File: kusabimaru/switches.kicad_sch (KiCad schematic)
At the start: 276 parts

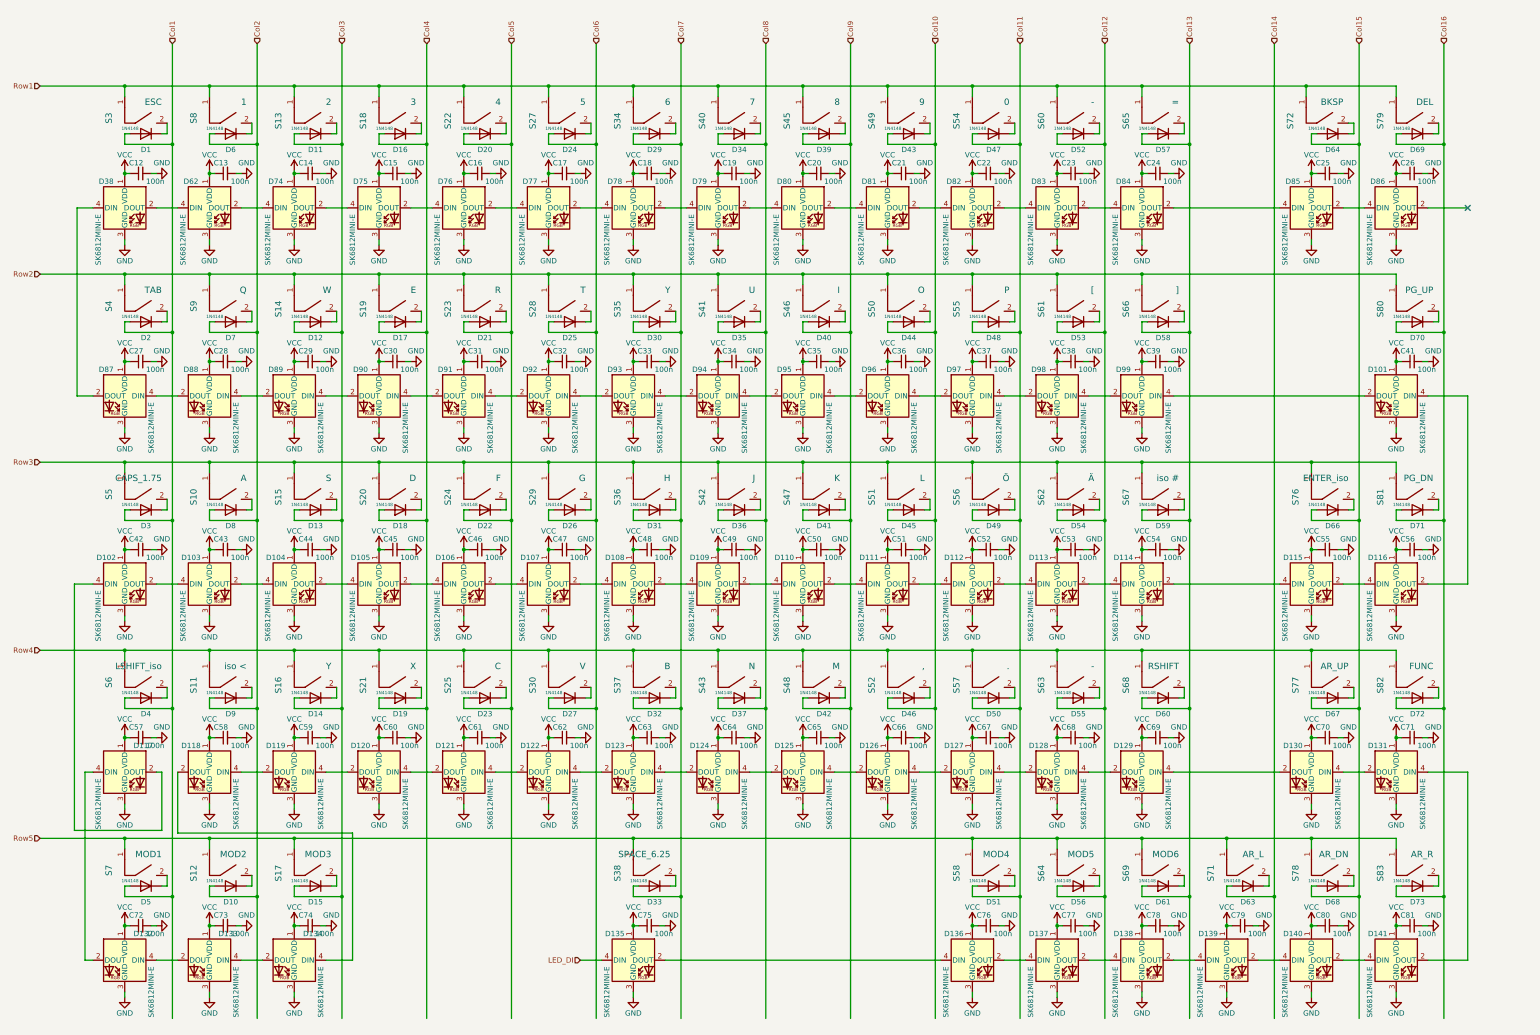
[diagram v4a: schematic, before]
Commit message: Updates to the PCB and the schematic.
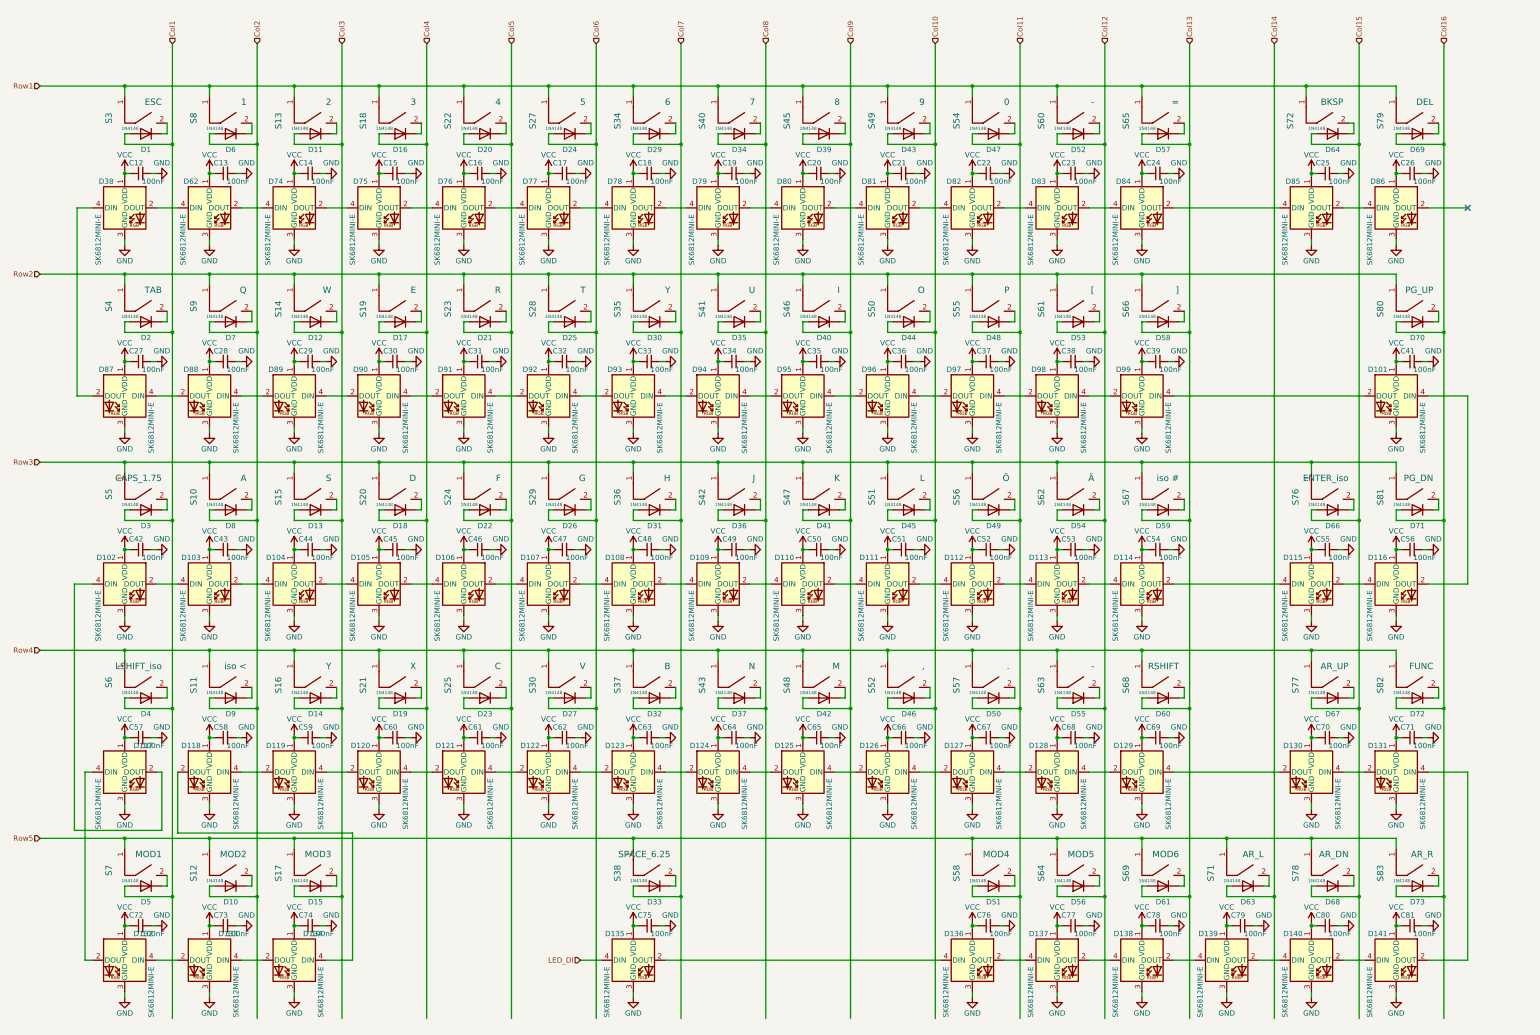
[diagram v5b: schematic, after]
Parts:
- C12, C13, C14, C15, C16, C17, C18, C19, C20, C21, C22, C23, C24, C25, C26, C27, C28, C29, C30, C31, C32, C33, C34, C35, C36, C37, C38, C39, C41, C42, C43, C44, C45, C46, C47, C48, C49, C50, C51, C52, C53, C54, C55, C56, C57, C58, C59, C60, C61, C62, C63, C64, C65, C66, C67, C68, C69, C70, C71, C72, C73, C74, C75, C76, C77, C78, C79, C80, C81: value 100n -> 100nF; LCSC (none) -> C14663; Shop-URL (none) -> https://jlcpcb.com/partdetail/Yageo-CC0603KRX7R9BB104/C14663
- D1, D10, D11, D12, D13, D14, D15, D16, D17, D18, D19, D2, D20, D21, D22, D23, D24, D25, D26, D27, D29, D3, D30, D31, D32, D33, D34, D35, D36, D37, D39, D4, D40, D41, D42, D43, D44, D45, D46, D47, D48, D49, D5, D50, D51, D52, D53, D54, D55, D56, D57, D58, D59, D6, D60, D61, D63, D64, D66, D67, D68, D69, D7, D70, D71, D72, D73, D8, D9: LCSC (none) -> C81598; Shop-URL (none) -> https://jlcpcb.com/partdetail/st_semtech-1N4148W/C81598
